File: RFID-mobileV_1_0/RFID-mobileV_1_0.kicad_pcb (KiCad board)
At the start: 2 copper layers, 50.7 x 89.5 mm, 54 parts, among them J1 USB_C_Receptacle_USB2.0, J2 Conn_01x05_Male, J3 Conn_01x05_Female, J4 Conn_01x05_Male, Q1 MMBT3904, SW1 SW_Push, U1 XC6206P332MR, U2 E22-400T22S, U3 STM32G030FxP, U4 LM321, U5 DW02, U6 TP4054

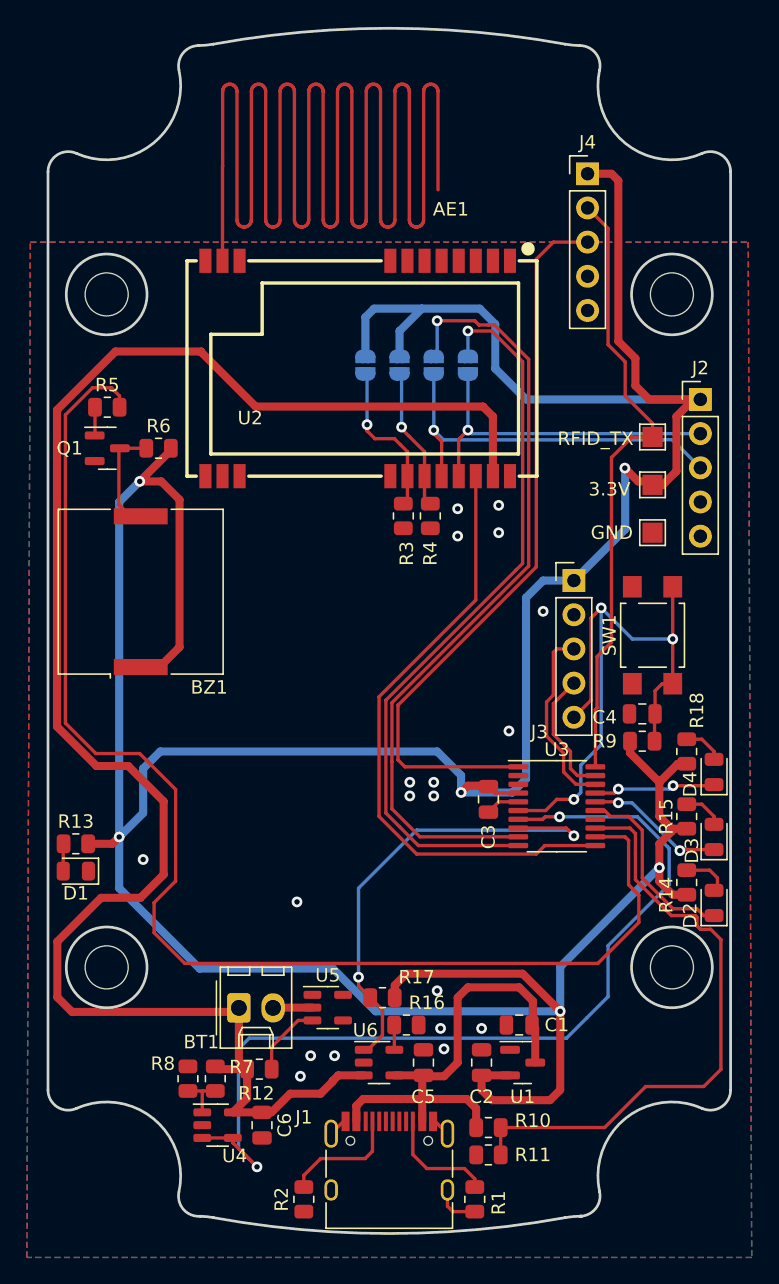
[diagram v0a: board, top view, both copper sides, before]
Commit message: update
remote DW02
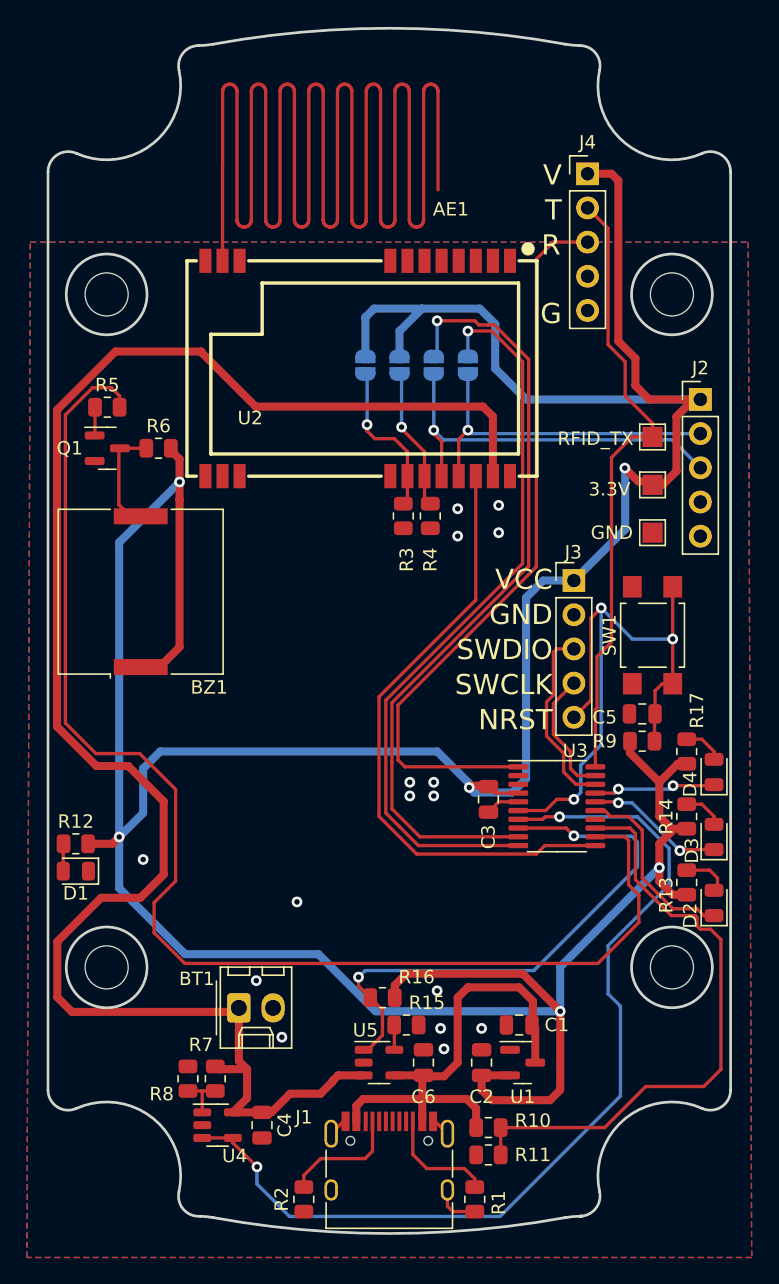
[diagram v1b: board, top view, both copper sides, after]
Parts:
- removed the R12 at (79.8, 158.5)
- removed the U5 at (84.8, 153.9)
- renumbered C6 to C4, C4 to C5, C5 to C6, R13 to R12, R14 to R13, R15 to R14, R16 to R15, R17 to R16, R18 to R17, U6 to U5
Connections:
- BT1 pad 2: Net-(BT1-Pad2) -> GND
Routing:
- net /CHAR_STAT: track 35.8 -> 42.2 mm
- net Net-(R12-Pad2): track 5.50 -> 0.00 mm
- net +3V3: track 294.6 -> 291.6 mm
- net Net-(BT1-Pad2): track 2.93 -> 0.00 mm
- net /BATT_moint: track 68.7 -> 71.1 mm
- net GND: vias 19 -> 16
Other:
- board text added: "G"
- board text added: "GND"
- board text added: "NRST"
- board text added: "R"
- board text added: "SWCLK"
- board text added: "SWDIO"
- board text added: "T"
- board text added: "V"
- board text added: "VCC"

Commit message: add jlcpcb
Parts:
- C5: value C -> 0.1uF

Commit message: update
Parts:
- removed BT1: Battery, Connector_Molex:Molex_KK-254_AE-6410-02A_1x02_P2.54mm_Vertical
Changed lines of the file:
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@@
     (property "Sheetfile" "RFID-mobileV_1_0.kicad_sch")
     (property "Sheetname" "")
+    (property "exclude_from_bom" "")
     (attr smd exclude_from_pos_files exclude_from_bom)
     (fp_text reference "U2" (at 3.428 8.255 unlocked) (layer "F.SilkS")
@@
       (offset (xyz 0 0 0))
       (scale (xyz 1 1 1))
-      (rotate (xyz 0 0 0))
-    )
-  )
-  (footprint "Connector_Molex:Molex_KK-254_AE-6410-02A_1x02_P2.54mm_Vertical" (layer "F.Cu")
-    (at 78.232 153.924)
-    (descr "Molex KK-254 Interconnect System, old/engineering part number: AE-6410-02A example for new part number: 22-27-2021, 2 Pins (http://www.molex.com/pdm_docs/sd/022272021_sd.pdf), generated with kicad-footprint-generator")
-    (tags "connector Molex KK-254 vertical")
-    (property "Sheetfile" "RFID-mobileV_1_0.kicad_sch")
-    (property "Sheetname" "")
-    (attr through_hole exclude_from_pos_files exclude_from_bom)
-    (fp_text reference "BT1" (at -3.1242 -2.159) (layer "F.SilkS")
-      (effects (font (size 1 1) (thickness 0.15)))
-    )
-    (fp_text value "Battery" (at 1.27 4.08) (layer "F.Fab")
-      (effects (font (size 1 1) (thickness 0.15)))
-    )
-    (fp_text user "${REFERENCE}" (at 1.27 -2.22) (layer "F.Fab")
-      (effects (font (size 1 1) (thickness 0.15)))
-    )
-    (fp_line (start 2.54 1.99) (end 2.54 2.99) (layer "F.SilkS") (width 0.12))
-    (fp_line (start 0 1.99) (end 0.25 1.46) (layer "F.SilkS") (width 0.12))
-    (fp_line (start -1.67 -2) (end -1.67 2) (layer "F.SilkS") (width 0.12))
-    (fp_line (start 0 1.99) (end 2.54 1.99) (layer "F.SilkS") (width 0.12))
-    (fp_line (start 3.92 2.99) (end 3.92 -3.03) (layer "F.SilkS") (width 0.12))
-    (fp_line (start 1.74 -2.43) (end 3.34 -2.43) (layer "F.SilkS") (width 0.12))
-    (fp_line (start 2.29 2.99) (end 2.29 1.99) (layer "F.SilkS") (width 0.12))
-    (fp_line (start 0.25 2.99) (end 0.25 1.99) (layer "F.SilkS") (width 0.12))
-    (fp_line (start 2.29 1.46) (end 2.54 1.99) (layer "F.SilkS") (width 0.12))
-    (fp_line (start 3.34 -2.43) (end 3.34 -3.03) (layer "F.SilkS") (width 0.12))
-    (fp_line (start 0.8 -2.43) (end 0.8 -3.03) (layer "F.SilkS") (width 0.12))
-    (fp_line (start 0 2.99) (end 0 1.99) (layer "F.SilkS") (width 0.12))
-    (fp_line (start -1.38 2.99) (end 3.92 2.99) (layer "F.SilkS") (width 0.12))
-    (fp_line (start -0.8 -3.03) (end -0.8 -2.43) (layer "F.SilkS") (width 0.12))
-    (fp_line (start 0.25 1.46) (end 2.29 1.46) (layer "F.SilkS") (width 0.12))
-    (fp_line (start -0.8 -2.43) (end 0.8 -2.43) (layer "F.SilkS") (width 0.12))
-    (fp_line (start 1.74 -3.03) (end 1.74 -2.43) (layer "F.SilkS") (width 0.12))
-    (fp_line (start 3.92 -3.03) (end -1.38 -3.03) (layer "F.SilkS") (width 0.12))
-    (fp_line (start -1.38 -3.03) (end -1.38 2.99) (layer "F.SilkS") (width 0.12))
-    (fp_line (start -1.77 3.38) (end 4.31 3.38) (layer "F.CrtYd") (width 0.05))
-    (fp_line (start -1.77 -3.42) (end -1.77 3.38) (layer "F.CrtYd") (width 0.05))
-    (fp_line (start 4.31 -3.42) (end -1.77 -3.42) (layer "F.CrtYd") (width 0.05))
-    (fp_line (start 4.31 3.38) (end 4.31 -3.42) (layer "F.CrtYd") (width 0.05))
-    (fp_line (start -0.562893 0) (end -1.27 0.5) (layer "F.Fab") (width 0.1))
-    (fp_line (start -1.27 -2.92) (end -1.27 2.88) (layer "F.Fab") (width 0.1))
-    (fp_line (start 3.81 2.88) (end 3.81 -2.92) (layer "F.Fab") (width 0.1))
-    (fp_line (start -1.27 -0.5) (end -0.562893 0) (layer "F.Fab") (width 0.1))
-    (fp_line (start -1.27 2.88) (end 3.81 2.88) (layer "F.Fab") (width 0.1))
-    (fp_line (start 3.81 -2.92) (end -1.27 -2.92) (layer "F.Fab") (width 0.1))
-    (pad "1" thru_hole roundrect (at 0 0) (size 1.74 2.19) (drill 1.19) (layers *.Cu *.Mask) (roundrect_rratio 0.1436781609)
-      (net 2 "+BATT") (pinfunction "+") (pintype "passive"))
-    (pad "2" thru_hole oval (at 2.54 0) (size 1.74 2.19) (drill 1.19) (layers *.Cu *.Mask)
-      (net 7 "GND") (pinfunction "-") (pintype "passive"))
-    (model "${KICAD6_3DMODEL_DIR}/Connector_Molex.3dshapes/Molex_KK-254_AE-6410-02A_1x02_P2.54mm_Vertical.wrl"
-      (offset (xyz 0 0 0))
-      (scale (xyz 1 1 1))

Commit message: fix BT1
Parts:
- added BT1: Battery, Connector_Molex:Molex_KK-254_AE-6410-02A_1x02_P2.54mm_Vertical, F.Cu at (78.4, 154.0)
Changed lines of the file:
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@@
+    )
+  )
+  (footprint "Connector_Molex:Molex_KK-254_AE-6410-02A_1x02_P2.54mm_Vertical" (layer "F.Cu")
+    (at 78.359 154.0256)
+    (descr "Molex KK-254 Interconnect System, old/engineering part number: AE-6410-02A example for new part number: 22-27-2021, 2 Pins (http://www.molex.com/pdm_docs/sd/022272021_sd.pdf), generated with kicad-footprint-generator")
+    (tags "connector Molex KK-254 vertical")
+    (property "Sheetfile" "RFID-mobileV_1_0.kicad_sch")
+    (property "Sheetname" "")
+    (property "exclude_from_bom" "")
+    (attr through_hole exclude_from_bom)
+    (fp_text reference "BT1" (at 1.27 -4.12) (layer "F.SilkS")
+      (effects (font (size 1 1) (thickness 0.15)))
+    )
+    (fp_text value "Battery" (at 1.27 4.08) (layer "F.Fab")
+      (effects (font (size 1 1) (thickness 0.15)))
+    )
+    (fp_text user "${REFERENCE}" (at 1.27 -2.22) (layer "F.Fab")
+      (effects (font (size 1 1) (thickness 0.15)))
+    )
+    (fp_line (start 3.92 2.99) (end 3.92 -3.03) (layer "F.SilkS") (width 0.12))
+    (fp_line (start 2.29 2.99) (end 2.29 1.99) (layer "F.SilkS") (width 0.12))
+    (fp_line (start 2.54 1.99) (end 2.54 2.99) (layer "F.SilkS") (width 0.12))
+    (fp_line (start -0.8 -3.03) (end -0.8 -2.43) (layer "F.SilkS") (width 0.12))
+    (fp_line (start -1.38 2.99) (end 3.92 2.99) (layer "F.SilkS") (width 0.12))
+    (fp_line (start 0.25 1.46) (end 2.29 1.46) (layer "F.SilkS") (width 0.12))
+    (fp_line (start 3.34 -2.43) (end 3.34 -3.03) (layer "F.SilkS") (width 0.12))
+    (fp_line (start -1.38 -3.03) (end -1.38 2.99) (layer "F.SilkS") (width 0.12))
+    (fp_line (start -1.67 -2) (end -1.67 2) (layer "F.SilkS") (width 0.12))
+    (fp_line (start 0.25 2.99) (end 0.25 1.99) (layer "F.SilkS") (width 0.12))
+    (fp_line (start -0.8 -2.43) (end 0.8 -2.43) (layer "F.SilkS") (width 0.12))
+    (fp_line (start 1.74 -2.43) (end 3.34 -2.43) (layer "F.SilkS") (width 0.12))
+    (fp_line (start 3.92 -3.03) (end -1.38 -3.03) (layer "F.SilkS") (width 0.12))
+    (fp_line (start 0 1.99) (end 0.25 1.46) (layer "F.SilkS") (width 0.12))
+    (fp_line (start 1.74 -3.03) (end 1.74 -2.43) (layer "F.SilkS") (width 0.12))
+    (fp_line (start 0.8 -2.43) (end 0.8 -3.03) (layer "F.SilkS") (width 0.12))
+    (fp_line (start 0 1.99) (end 2.54 1.99) (layer "F.SilkS") (width 0.12))
+    (fp_line (start 2.29 1.46) (end 2.54 1.99) (layer "F.SilkS") (width 0.12))
+    (fp_line (start 0 2.99) (end 0 1.99) (layer "F.SilkS") (width 0.12))
+    (fp_line (start 4.31 -3.42) (end -1.77 -3.42) (layer "F.CrtYd") (width 0.05))
+    (fp_line (start 4.31 3.38) (end 4.31 -3.42) (layer "F.CrtYd") (width 0.05))
+    (fp_line (start -1.77 3.38) (end 4.31 3.38) (layer "F.CrtYd") (width 0.05))
+    (fp_line (start -1.77 -3.42) (end -1.77 3.38) (layer "F.CrtYd") (width 0.05))
+    (fp_line (start 3.81 -2.92) (end -1.27 -2.92) (layer "F.Fab") (width 0.1))
+    (fp_line (start -1.27 2.88) (end 3.81 2.88) (layer "F.Fab") (width 0.1))
+    (fp_line (start 3.81 2.88) (end 3.81 -2.92) (layer "F.Fab") (width 0.1))
+    (fp_line (start -0.562893 0) (end -1.27 0.5) (layer "F.Fab") (width 0.1))
+    (fp_line (start -1.27 -0.5) (end -0.562893 0) (layer "F.Fab") (width 0.1))
+    (fp_line (start -1.27 -2.92) (end -1.27 2.88) (layer "F.Fab") (width 0.1))
+    (pad "1" thru_hole roundrect (at 0 0) (size 1.74 2.19) (drill 1.19) (layers *.Cu *.Mask) (roundrect_rratio 0.143678)
+      (net 2 "+BATT") (pinfunction "+") (pintype "passive"))
+    (pad "2" thru_hole oval (at 2.54 0) (size 1.74 2.19) (drill 1.19) (layers *.Cu *.Mask)
+      (net 7 "GND") (pinfunction "-") (pintype "passive"))
+    (model "${KICAD6_3DMODEL_DIR}/Connector_Molex.3dshapes/Molex_KK-254_AE-6410-02A_1x02_P2.54mm_Vertical.wrl"
+      (offset (xyz 0 0 0))
+      (scale (xyz 1 1 1))
+      (rotate (xyz 0 0 0))
     )
   )

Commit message: Update RFID-mobileV_1_0.kicad_pcb
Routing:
- net +3V3: track 291.6 -> 289.1 mm, vias 6 -> 5
- net GND: vias 16 -> 11
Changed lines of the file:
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@@
   (segment (start 112.009 108.717) (end 112.522 108.717) (width 0.6) (layer "F.Cu") (net 4))
   (segment (start 89.8125 152.2495) (end 90.678 151.384) (width 0.6) (layer "F.Cu") (net 4))
-  (segment (start 68.834 141.732) (end 69.342 141.224) (width 0.6) (layer "F.Cu") (net 4))
   (segment (start 107.2915 134.9775) (end 109.474 137.16) (width 0.6) (layer "F.Cu") (net 4))
   (segment (start 73.825 116.162562) (end 73.822881 116.164681) (width 0.6) (layer "F.Cu") (net 4))
@@
   (segment (start 110.3865 140.6125) (end 111.506 140.6125) (width 0.6) (layer "F.Cu") (net 4))
   (segment (start 110.744 109.982) (end 112.009 108.717) (width 0.6) (layer "F.Cu") (net 4))
-  (segment (start 67.031 141.732) (end 68.834 141.732) (width 0.6) (layer "F.Cu") (net 4))
   (segment (start 98.3765 158.938) (end 96.266 158.938) (width 0.6) (layer "F.Cu") (net 4))
   (segment (start 72.3422 128.6002) (end 70.9422 128.6002) (width 0.6) (layer "F.Cu") (net 4))
@@
   (via (at 109.474 143.51) (size 0.8) (drill 0.4) (layers "F.Cu" "B.Cu") (net 4))
   (via (at 73.825 114.85) (size 0.8) (drill 0.4) (layers "F.Cu" "B.Cu") (net 4))
-  (via (at 69.342 141.224) (size 0.8) (drill 0.4) (layers "F.Cu" "B.Cu") (net 4))
   (via (at 102.108 154.178) (size 0.8) (drill 0.4) (layers "F.Cu" "B.Cu") (net 4))
   (via (at 106.9086 113.8174) (size 0.8) (drill 0.4) (layers "F.Cu" "B.Cu") (net 4))
@@
   (segment (start 86.157996 162.355) (end 86.002996 162.355) (width 0.25) (layer "F.Cu") (net 7))
   (segment (start 92.812996 162.355) (end 93.727996 163.27) (width 0.25) (layer "F.Cu") (net 7))
-  (via (at 71.12 142.9004) (size 0.8) (drill 0.4) (layers "F.Cu" "B.Cu") (free) (net 7))
   (via (at 79.525 151.9) (size 0.8) (drill 0.4) (layers "F.Cu" "B.Cu") (free) (net 7))
   (via (at 92.964 152.654) (size 0.8) (drill 0.4) (layers "F.Cu" "B.Cu") (free) (net 7))
   (via (at 94.488 118.872) (size 0.8) (drill 0.4) (layers "F.Cu" "B.Cu") (free) (net 7))
   (via (at 96.266 155.448) (size 0.8) (drill 0.4) (layers "F.Cu" "B.Cu") (free) (net 7))
-  (via (at 92.71 137.16) (size 0.8) (drill 0.4) (layers "F.Cu" "B.Cu") (free) (net 7))
   (via (at 97.536 116.586) (size 0.8) (drill 0.4) (layers "F.Cu" "B.Cu") (free) (net 7))
   (via (at 82.55 146.05) (size 0.8) (drill 0.4) (layers "F.Cu" "B.Cu") (free) (net 7))
-  (via (at 92.71 138.176) (size 0.8) (drill 0.4) (layers "F.Cu" "B.Cu") (free) (net 7))
   (via (at 94.488 116.84) (size 0.8) (drill 0.4) (layers "F.Cu" "B.Cu") (free) (net 7))
   (via (at 81.425 156.1) (size 0.8) (drill 0.4) (layers "F.Cu" "B.Cu") (free) (net 7))
-  (via (at 90.932 138.176) (size 0.8) (drill 0.4) (layers "F.Cu" "B.Cu") (free) (net 7))
   (via (at 93.472 156.972) (size 0.8) (drill 0.4) (layers "F.Cu" "B.Cu") (free) (net 7))
-  (via (at 90.932 137.16) (size 0.8) (drill 0.4) (layers "F.Cu" "B.Cu") (free) (net 7))
   (via (at 93.218 155.448) (size 0.8) (drill 0.4) (layers "F.Cu" "B.Cu") (free) (net 7))
   (via (at 97.536 118.618) (size 0.8) (drill 0.4) (layers "F.Cu" "B.Cu") (free) (net 7))
@@
     (connect_pads (clearance 0.508))
     (min_thickness 0.254) (filled_areas_thickness no)
-    (fill yes (thermal_gap 0.508) (thermal_bridge_width 0.508) (smoothing chamfer) (radius 1.5) (island_removal_mode 1) (island_area_min 0))
+    (fill (thermal_gap 0.508) (thermal_bridge_width 0.508) (smoothing chamfer) (radius 1.5) (island_removal_mode 1) (island_area_min 0))
     (polygon
       (pts
